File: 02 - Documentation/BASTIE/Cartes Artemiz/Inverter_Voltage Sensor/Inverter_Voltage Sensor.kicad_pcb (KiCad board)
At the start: 2 copper layers, 61 x 68.6 mm, 18 parts, among them J1 3P Droit 22-11-2032, K1 SSR CPC1394GR

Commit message: Kicadlib + Modifs cartes
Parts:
- removed the ? at (132.1, 119.4)
- removed REF**: MountingHole_3.2mm_M3_DIN965_Pad, MountingHole:MountingHole_3.2mm_M3_DIN965_Pad
- added ?: , , F.Cu at (95.9, 85.7)
- added ?: , , F.Cu at (132.1, 120.0)
- added R4: 3k9, EPSA_lib:RESC3216X70N, F.Cu at (127.6, 92.1)
- added R8: 8k2, EPSA_lib:RESC3216X70N, F.Cu at (127.0, 87.0)
- added R9: 8k2, EPSA_lib:RESC3216X70N, F.Cu at (127.6, 95.9)
- R1: value Résistance RK73H2BLTDD2152F -> 820k
- R2: value Résistance RK73H2BLTDD2152F -> 1k2
- R3: value Résistance RK73H2BLTDD2152F -> 1k
- R5: value Résistance RK73H2BLTDD2152F -> 33k
- R6: value Résistance RK73H2BLTDD2152F -> 2k7
- R7: value Résistance RK73H2BLTDD2152F -> 2k
- TP1, TP2: value TestPoint -> type="R" model="TestPoint" lib=""
- moved R7 2.29 mm to (123.2, 87.0), turned to -90 degrees
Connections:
- net Net-CP1-Pad3 renamed Net-(CP1-IN-)
- net Net-CP1-Pad4 renamed Net-(CP1-IN+)
- K1 pad 3: Exit -> Raw_Exit
- R7 pad 2: Exit -> Raw_Exit
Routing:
- net GND: track 40.5 -> 0.00 mm
- net Raw_Exit: track 0.00 -> 14.2 mm
- net +5VA: track 23.8 -> 29.6 mm
- net Exit: track 19.9 -> 15.2 mm
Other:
- board text added: "EPSA Inverter Voltage Sensor V1.0"
- board text removed: "EPSA Inverter Voltage Sensor V2.0"

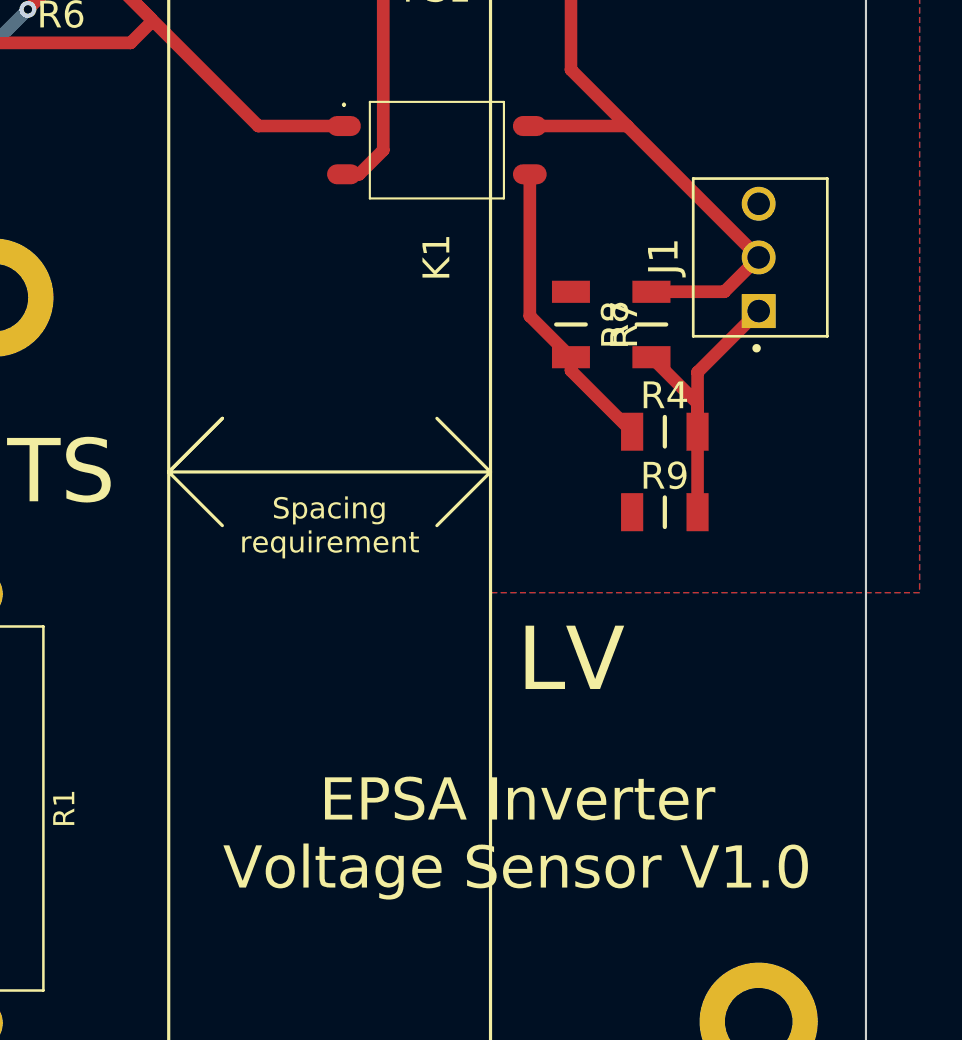
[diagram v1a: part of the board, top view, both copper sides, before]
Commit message: Vérification PCBs + Fichiers Fabrication
Préparation pour production des PCBs
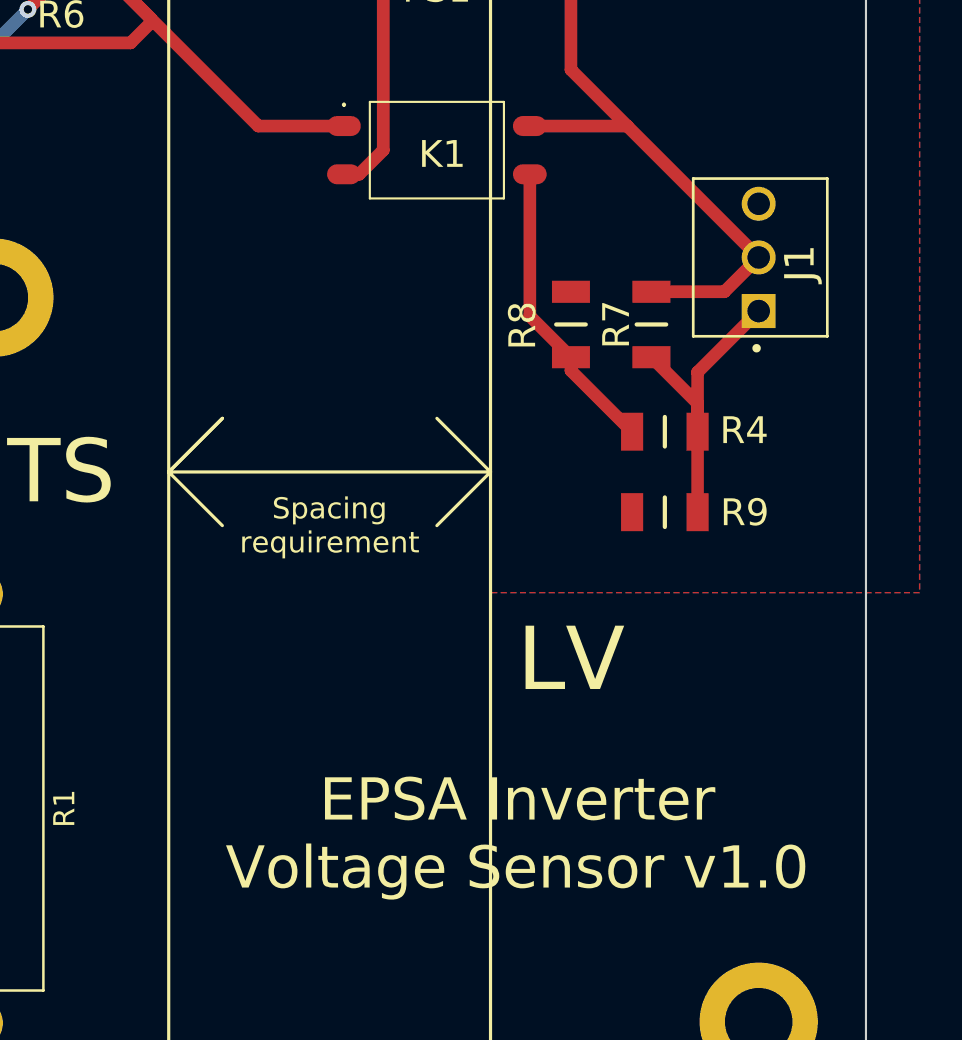
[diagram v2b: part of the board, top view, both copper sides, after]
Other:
- board text added: "EPSA Inverter Voltage Sensor v1.0"
- board text removed: "EPSA Inverter Voltage Sensor V1.0"
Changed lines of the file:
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@@
 			(drillshape 0)
 			(scaleselection 1)
-			(outputdirectory "Cirly/")
+			(outputdirectory "../Cirly/Inverter Voltage/")
 		)
 	)
@@
 		(tags "Relay or Contactor")
 		(property "Reference" "K1"
-			(at 5.08 0 90)
+			(at 0.2032 -0.254 180)
 			(layer "F.SilkS")
 			(effects
@@
 		(tags "Resistor")
 		(property "Reference" "R7"
-			(at 0 -2.54 90)
+			(at 0 -2.159 90)
 			(layer "F.SilkS")
 			(effects
@@
 		(tags "Resistor")
 		(property "Reference" "R9"
-			(at -0.011901 -1.701971 0)
+			(at 3.7846 0.0254 0)
 			(layer "F.SilkS")
 			(effects
@@
 		(tags "Resistor")
 		(property "Reference" "R4"
-			(at -0.011901 -1.701971 0)
+			(at 3.7592 -0.0508 0)
 			(layer "F.SilkS")
 			(effects
@@
 		(at 132.08 86.36 90)
 		(property "Reference" "J1"
-			(at 2.585 -4.489 90)
+			(at 2.2606 1.9558 90)
 			(layer "F.SilkS")
 			(effects
@@
 		(tags "Resistor")
 		(property "Reference" "R8"
-			(at -0.011901 -1.701971 -90)
+			(at -0.0508 -6.096 -90)
 			(layer "F.SilkS")
 			(effects
@@
 		)
 	)
-	(gr_text "EPSA Inverter\nVoltage Sensor V1.0"
+	(gr_text "EPSA Inverter\nVoltage Sensor v1.0"
 		(at 120.65 111.125 0)
 		(layer "F.SilkS")
